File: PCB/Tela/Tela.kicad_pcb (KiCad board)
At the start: 2 copper layers, 93 x 70 mm, 9 parts, among them J1 Conn_01x04_Female, J2 Micro_SD_Card, U1 LM2596S-5, U2 ESP32

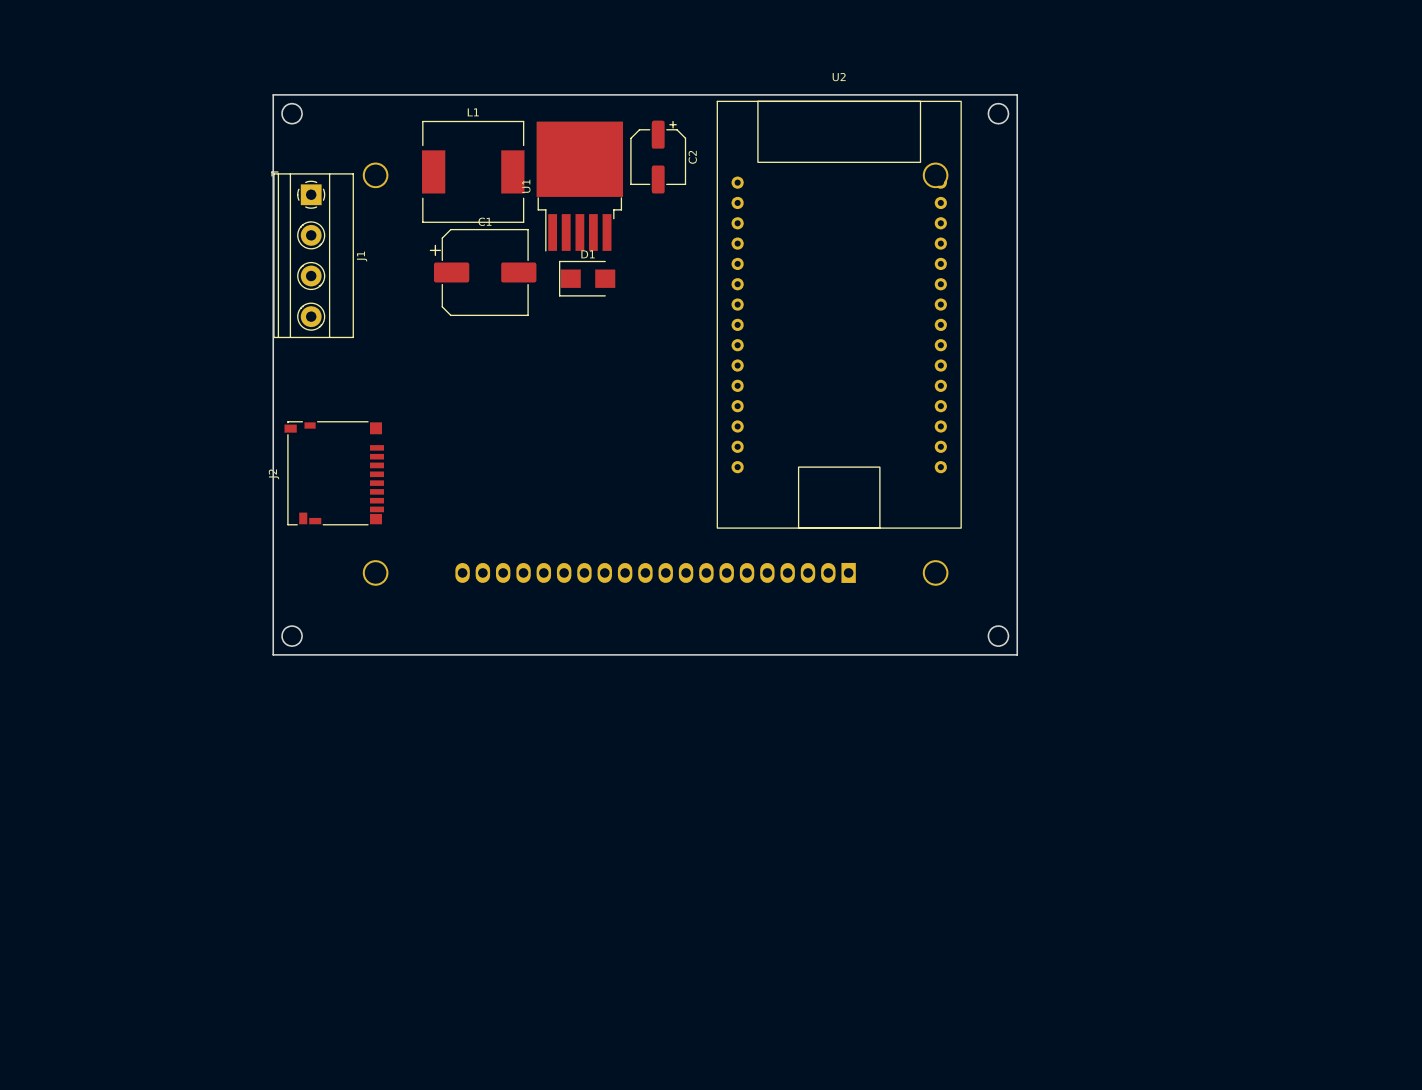
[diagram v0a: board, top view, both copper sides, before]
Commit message: adição dos footprint do modulo de can, adição dos botoes, e desenho de areas no silkscreen
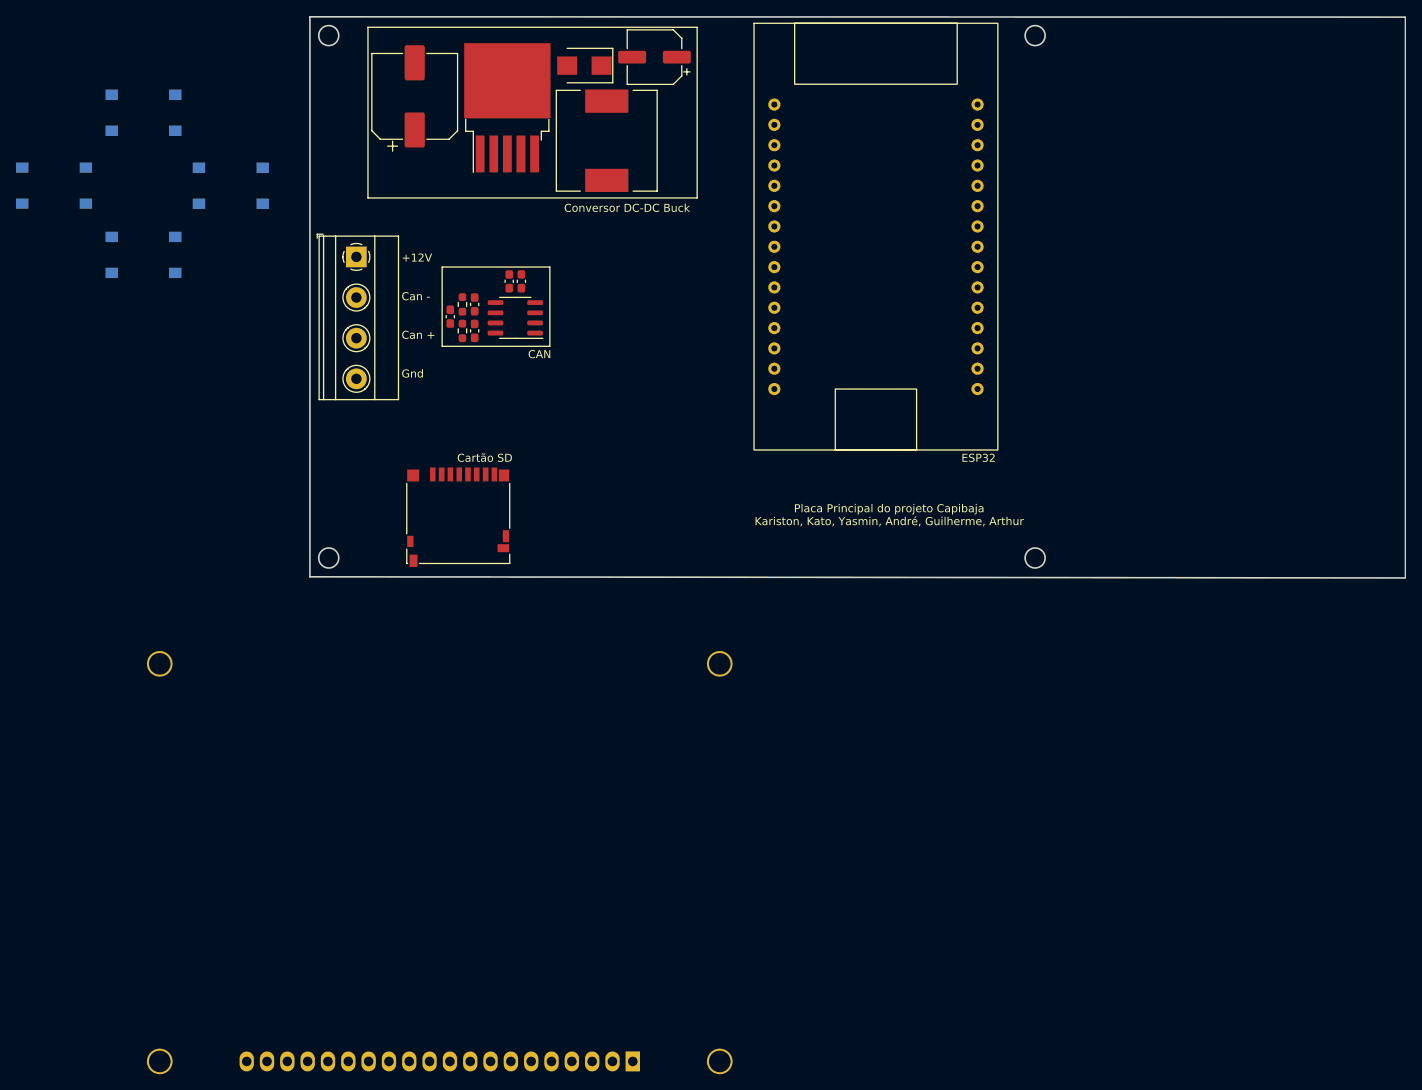
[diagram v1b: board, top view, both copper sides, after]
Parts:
- added C3: 100nF, Capacitor_SMD:C_0603_1608Metric_Pad1.08x0.95mm_HandSolder, F.Cu at (125.7, 81.4)
- added C4: 47nF, Capacitor_SMD:C_0603_1608Metric_Pad1.08x0.95mm_HandSolder, F.Cu at (127.3, 81.4)
- added C5: 100pF, Capacitor_SMD:C_0603_1608Metric_Pad1.08x0.95mm_HandSolder, F.Cu at (121.4, 87.6)
- added C6: 100pF, Capacitor_SMD:C_0603_1608Metric_Pad1.08x0.95mm_HandSolder, F.Cu at (121.4, 84.3)
- added C7: 4,7uF, Capacitor_SMD:C_0603_1608Metric_Pad1.08x0.95mm_HandSolder, F.Cu at (118.4, 85.8)
- added R1: 60, Resistor_SMD:R_0603_1608Metric_Pad0.98x0.95mm_HandSolder, F.Cu at (119.9, 87.6)
- added R2: 60, Resistor_SMD:R_0603_1608Metric_Pad0.98x0.95mm_HandSolder, F.Cu at (119.9, 84.3)
- added SW1: SW_Push, Button_Switch_SMD:SW_SPST_PTS645, B.Cu at (80.0, 60.3)
- added SW2: SW_Push, Button_Switch_SMD:SW_SPST_PTS645, B.Cu at (68.8, 69.5)
- added SW3: SW_Push, Button_Switch_SMD:SW_SPST_PTS645, B.Cu at (90.9, 69.5)
- added SW4: SW_Push, Button_Switch_SMD:SW_SPST_PTS645, B.Cu at (80.0, 78.1)
- added U3: TJA1051T-3, Package_SO:SOIC-8_3.9x4.9mm_P1.27mm, F.Cu at (126.5, 86.0)
- moved DS1 66.8 mm to (141.2, 178.9)
- moved D1 26.6 mm to (135.1, 54.5), turned to 180 degrees
- moved C1 23.7 mm to (113.9, 58.3), turned to 90 degrees
- moved L1 17.1 mm to (137.9, 63.9), turned to -90 degrees
- moved J2 16.4 mm to (119.4, 110.9), turned to 180 degrees
- moved U1 13.4 mm to (125.5, 59.7)
- moved C2 12.5 mm to (143.9, 53.4), turned to 180 degrees
- moved U2 10.8 mm to (171.6, 77.1)
- moved J1 9.61 mm to (106.6, 78.4)
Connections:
- J1 pad 2: /Can+ -> /Can-
- J1 pad 3: /Can- -> /Can+
- U2 pad 16: unconnected-(U2-Pad16) -> +3.3V
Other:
- board size 93 x 70 mm -> 136.9 x 70.1 mm
- board text added: "+12V Can - Can + Gnd"
- board text added: "CAN"
- board text added: "Cartão SD"
- board text added: "Conversor DC-DC Buck"
- board text added: "ESP32"
- board text added: "Placa Principal do projeto Capibaja Kariston, Kato, Yasmin, André, Guilherme, Arthur"

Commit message: imagens
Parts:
- moved SW1 132.1 mm to (212.1, 61.7)
- moved SW3 132.1 mm to (223.0, 70.9)
- moved SW4 132.1 mm to (212.1, 79.5)
- moved SW2 132.1 mm to (200.9, 70.8)
- moved DS1 81.8 mm to (178.8, 106.3)
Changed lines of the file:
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@@
   )
   (footprint "Button_Switch_SMD:SW_SPST_PTS645" (layer "B.Cu")
-    (at 80.026 78.123 180)
+    (at 212.09 79.502 180)
     (descr "C&K Components SPST SMD PTS645 Series 6mm Tact Switch")
     (tags "SPST Button Switch")
@@
   )
   (footprint "Button_Switch_SMD:SW_SPST_PTS645" (layer "B.Cu")
-    (at 80.026 60.343 180)
+    (at 212.09 61.722 180)
     (descr "C&K Components SPST SMD PTS645 Series 6mm Tact Switch")
     (tags "SPST Button Switch")
@@
   )
   (footprint "Button_Switch_SMD:SW_SPST_PTS645" (layer "B.Cu")
-    (at 68.85 69.463 180)
+    (at 200.914 70.842 180)
     (descr "C&K Components SPST SMD PTS645 Series 6mm Tact Switch")
     (tags "SPST Button Switch")
@@
   )
   (footprint "Display:AG12864E" (layer "B.Cu")
-    (at 141.194 178.9435 90)
+    (at 178.786 106.2995 90)
     (descr "STN/FSTN LCD 128x64 dot https://www.digchip.com/datasheets/parts/datasheet/1121/AG-12864E-pdf.php")
     (tags "AG12864E Graphics Display 128x64 Ampire")
@@
   )
   (footprint "Button_Switch_SMD:SW_SPST_PTS645" (layer "B.Cu")
-    (at 90.948 69.487 180)
+    (at 223.012 70.866 180)
     (descr "C&K Components SPST SMD PTS645 Series 6mm Tact Switch")
     (tags "SPST Button Switch")
@@
     (effects (font (size 1 1) (thickness 0.15)))
   )
-  (gr_text "+12V\n\n\nCan -\n\n\nCan +\n\n\nGnd" (at 112.284 85.743) (layer "F.SilkS")
+  (gr_text "+12V\n\n\nCan -\n\n\nCan +\n\n\nGnd" (at 111.76 85.743) (layer "F.SilkS")
     (effects (font (size 1 1) (thickness 0.2)) (justify left))
   )
